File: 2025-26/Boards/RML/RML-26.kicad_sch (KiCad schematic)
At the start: 30 parts, among them J1 043045-0412, Q1 DMP2035U-7, Q3 UJ3N065080K3S, Q4 DMN2056U, Q5 AO3401A, U1 H11L1M, U2 NE555D

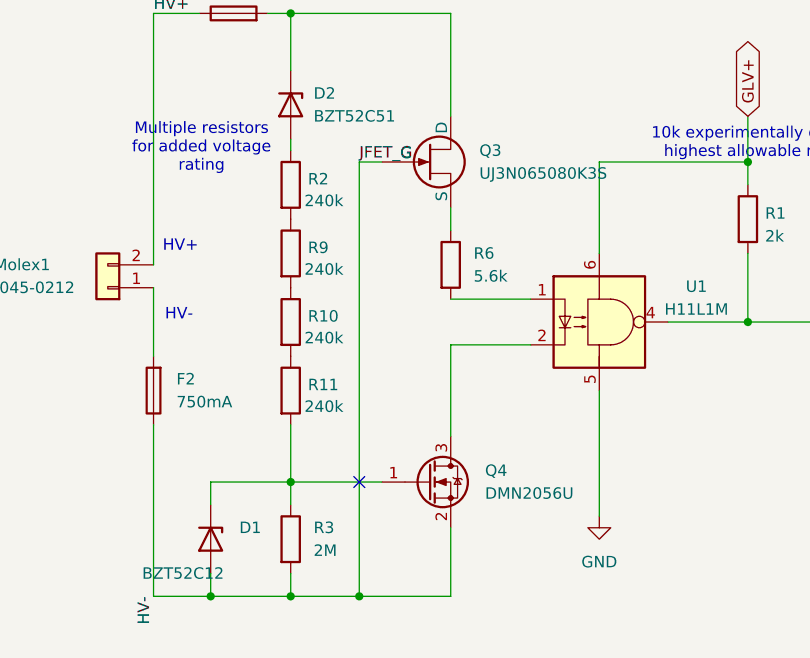
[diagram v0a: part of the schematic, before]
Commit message: Updated VIL and RML
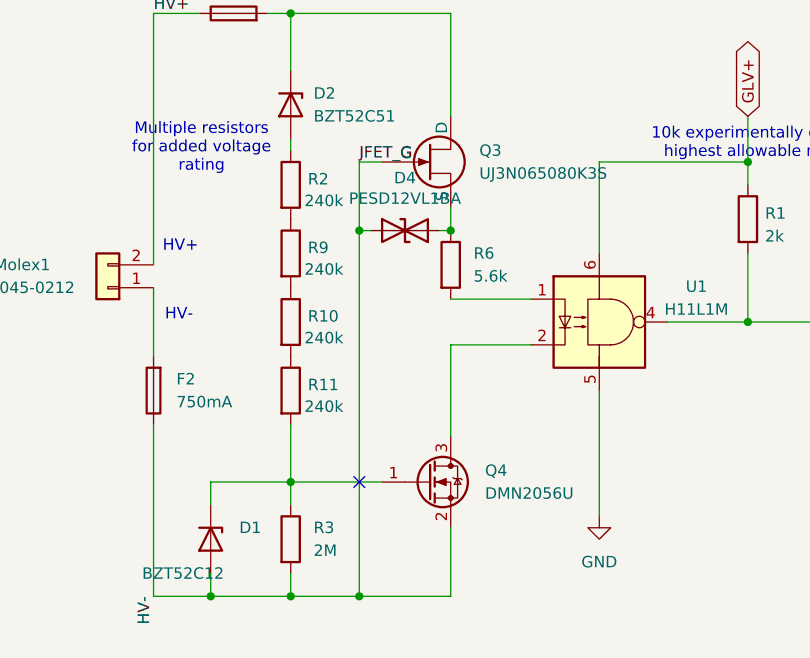
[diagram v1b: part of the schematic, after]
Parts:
- added D4: PESD12VL1BA, Diode_SMD:D_SOD-323, symbol Diode:1.5KExxCA
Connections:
- net HV-: now also D4.2 (A2)
- net at Q3.3 (S), R6.1: now also D4.1 (A1)
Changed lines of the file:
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@@
 	)
 	(junction
+		(at 69.85 76.2)
+		(diameter 0)
+		(color 0 0 0 0)
+	)
+	(junction
 		(at 157.48 44.45)
 		(diameter 0)
@@
 	)
 	(junction
+		(at 59.69 76.2)
+		(diameter 0)
+		(color 0 0 0 0)
+	)
+	(junction
 		(at 157.48 41.91)
 		(diameter 0)
@@
 	(wire
 		(pts
-			(xy 59.69 68.58) (xy 59.69 116.84)
+			(xy 59.69 68.58) (xy 59.69 76.2)
 		)
 		(stroke
@@
 	(wire
 		(pts
+			(xy 68.58 76.2) (xy 69.85 76.2)
+		)
+		(stroke
+			(width 0)
+			(type default)
+		)
+	)
+	(wire
+		(pts
 			(xy 157.48 41.91) (xy 157.48 44.45)
 		)
@@
 	(wire
 		(pts
+			(xy 59.69 76.2) (xy 60.96 76.2)
+		)
+		(stroke
+			(width 0)
+			(type default)
+		)
+	)
+	(wire
+		(pts
 			(xy 36.83 52.07) (xy 41.91 52.07)
 		)
@@
 	(wire
 		(pts
+			(xy 59.69 76.2) (xy 59.69 116.84)
+		)
+		(stroke
+			(width 0)
+			(type default)
+		)
+	)
+	(wire
+		(pts
 			(xy 102.87 68.58) (xy 102.87 71.12)
 		)
@@
 					(unit 1)
 				)
+			)
+		)
+	)
+	(symbol
+		(lib_id "Diode:1.5KExxCA")
+		(at 64.77 76.2 0)
+		(mirror y)
+		(unit 1)
+		(exclude_from_sim no)
+		(in_bom yes)
+		(on_board yes)
+		(dnp no)
+		(property "Reference" "D4"
+			(at 64.77 70.358 0)
+			(effects
+				(font
+					(size 1.27 1.27)
+				)
+			)
+		)
+		(property "Value" "PESD12VL1BA"
+			(at 64.77 72.644 0)
+			(effects
+				(font
+					(size 1.27 1.27)
+				)
+			)
+		)
+		(property "Footprint" "Diode_SMD:D_SOD-323"
+			(at 64.77 81.28 0)
+			(effects
+				(font
+					(size 1.27 1.27)
+				)
+				(hide yes)
+			)
+		)
+		(property "Datasheet" "https://www.vishay.com/docs/88301/15ke.pdf"
+			(at 64.77 76.2 0)
+			(effects
+				(font
+					(size 1.27 1.27)
+				)
+				(hide yes)
+			)
+		)
+		(property "Description" "1500W bidirectional TVS diode, DO-201AE"
+			(at 64.77 76.2 0)
+			(effects
+				(font
+					(size 1.27 1.27)
+				)
+				(hide yes)
+			)
+		)
+		(pin "1"
+		)
+		(pin "2"
+		)
+		(instances
+			(project "RML-26"
+				(path "/d0262e13-a8ab-42db-962e-1ef7dd9c8d4a"
+					(reference "D4")
+					(unit 1)
+				)
